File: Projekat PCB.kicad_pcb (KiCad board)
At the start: 2 copper layers, 106 x 110 mm, 84 parts, among them J1 PJ-002A, J3 MSD-3-A, J4 MD-30SM, P1 ICSP, P2 LCD-H, P3 USB_B, SW1 SW_SPST, U1 LM334Z, U2 LM317T_TO220, U3 MCP6022-I/SN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

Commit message: proba
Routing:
- net Net-(JP3-A): track 31.8 -> 35.8 mm
- net VBUS: track 22.2 -> 24.7 mm
- net Net-(J1-Pad2): track 43.6 -> 46.1 mm
- net VCC: track 184.4 -> 186.6 mm
- net Net-(SW1-A): track 8.28 -> 9.81 mm
- net /Power/VAA: track 32.1 -> 33.3 mm
- net Net-(R1-Pad1): track 10.3 -> 11.4 mm
- net Net-(P2-Pin_3): track 39.7 -> 40.5 mm
- net /MicroSD card reader/3.3V: track 62.8 -> 63.6 mm
- net Net-(J3-CLK): track 17.1 -> 16.4 mm
- net VCCIO: track 44.6 -> 45.3 mm
- net /Microcontroller/VPP: track 47.8 -> 48.4 mm

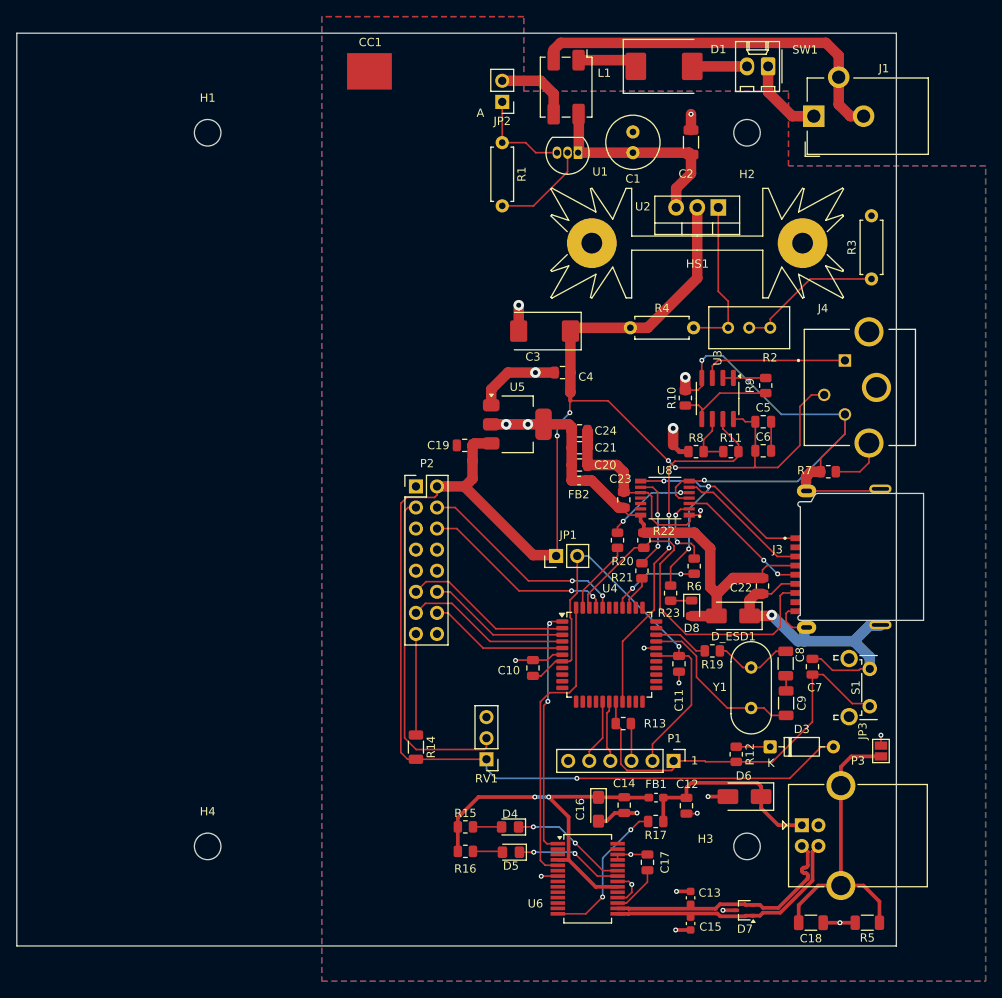
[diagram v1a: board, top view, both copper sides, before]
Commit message: Dodavanje stiching via
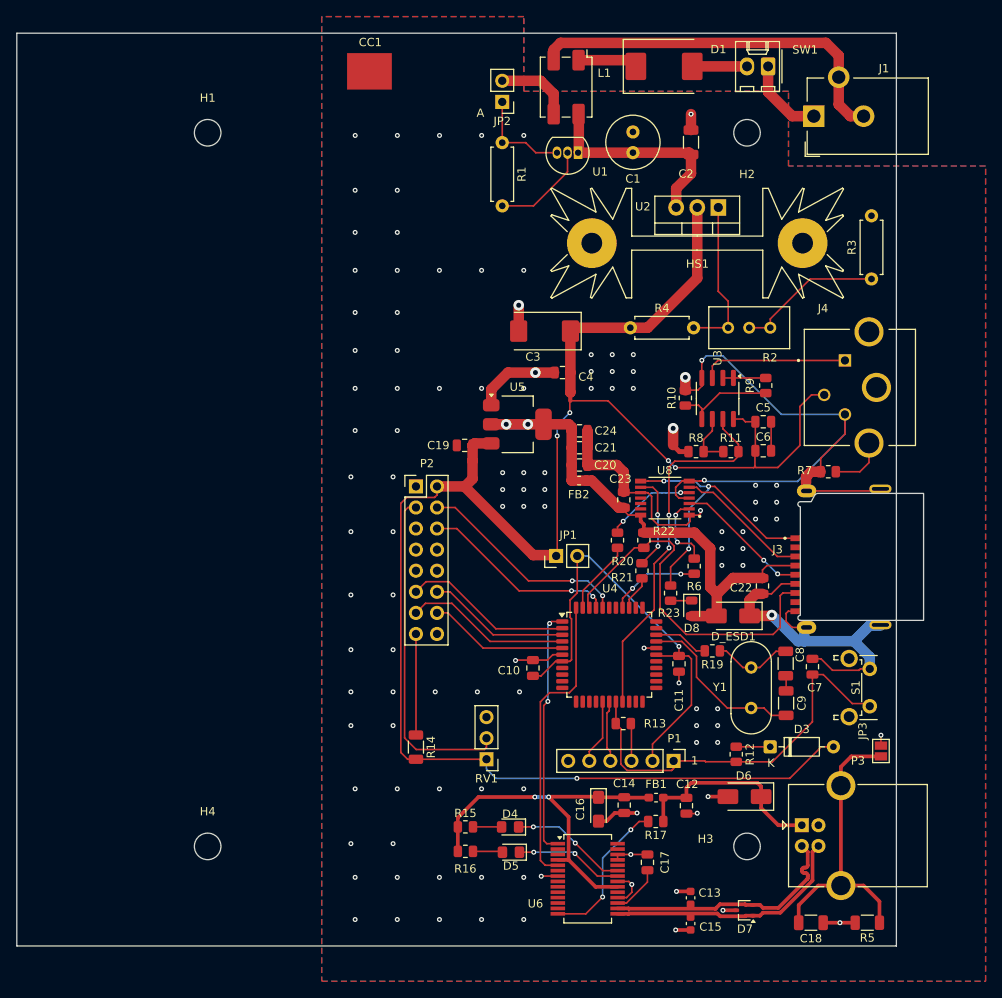
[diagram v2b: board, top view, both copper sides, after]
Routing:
- net GND: vias 23 -> 116
